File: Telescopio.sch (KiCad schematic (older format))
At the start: 18 parts, among them CON1 BARREL_JACK, P1 CONN_01X03, P10 CONN_01X08, P12 CONN_01X04, P13 CONN_01X04, P2 CONN_01X03, P3 CONN_01X05, P4 CONN_01X19, P5 CONN_01X19, P50 CONN_01X04, P51 CONN_01X10, P7 CONN_01X08, P8 CONN_01X08, P9 CONN_01X08

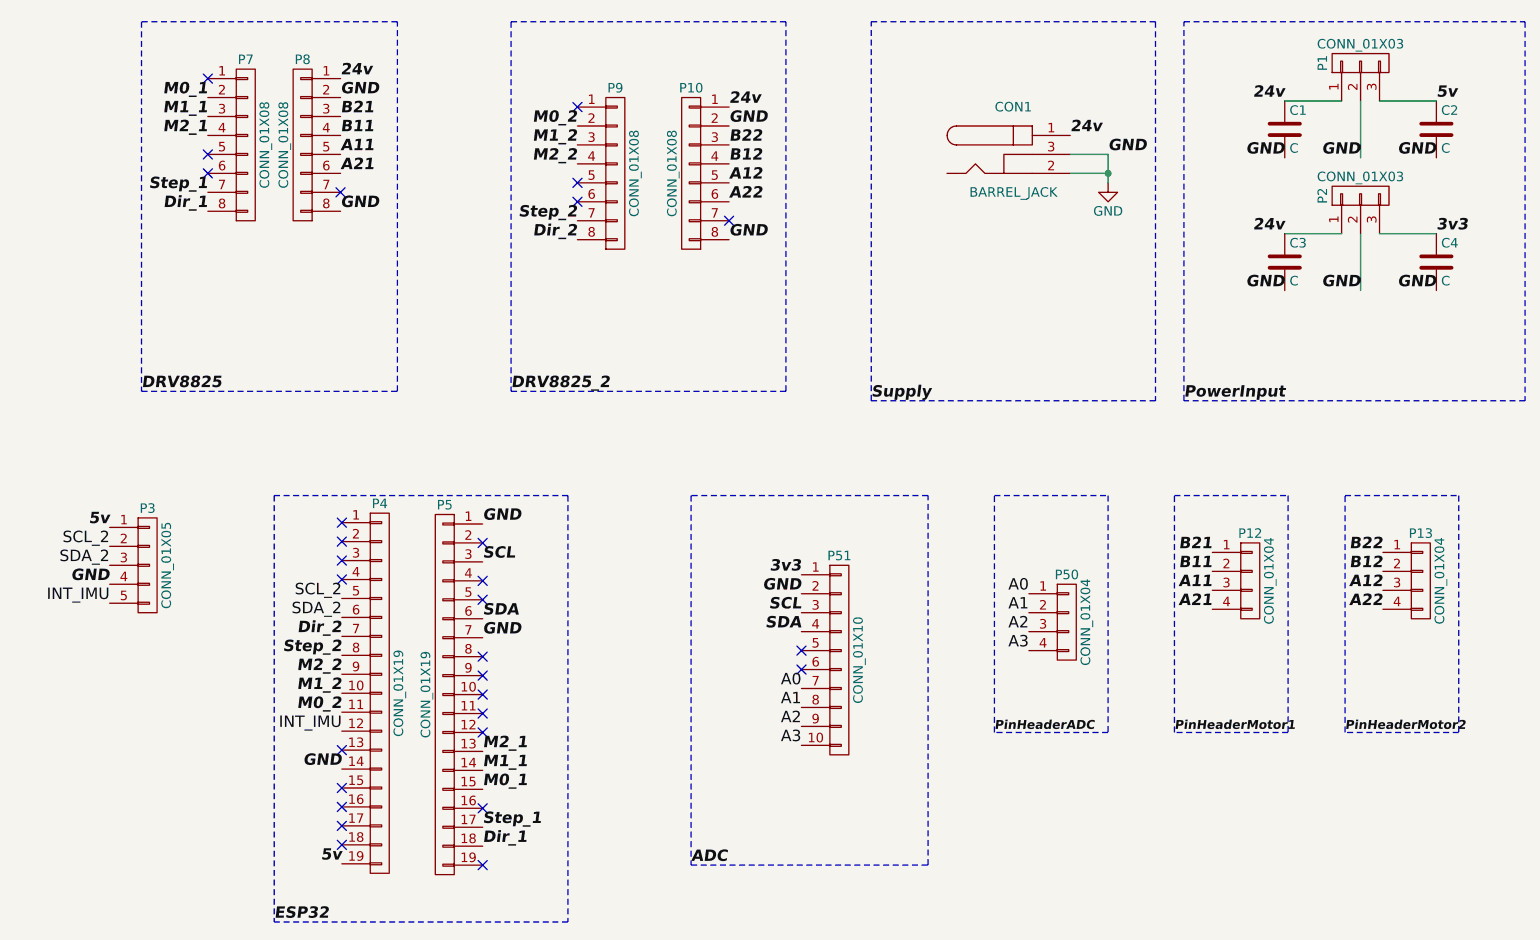
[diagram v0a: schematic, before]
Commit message: button reset
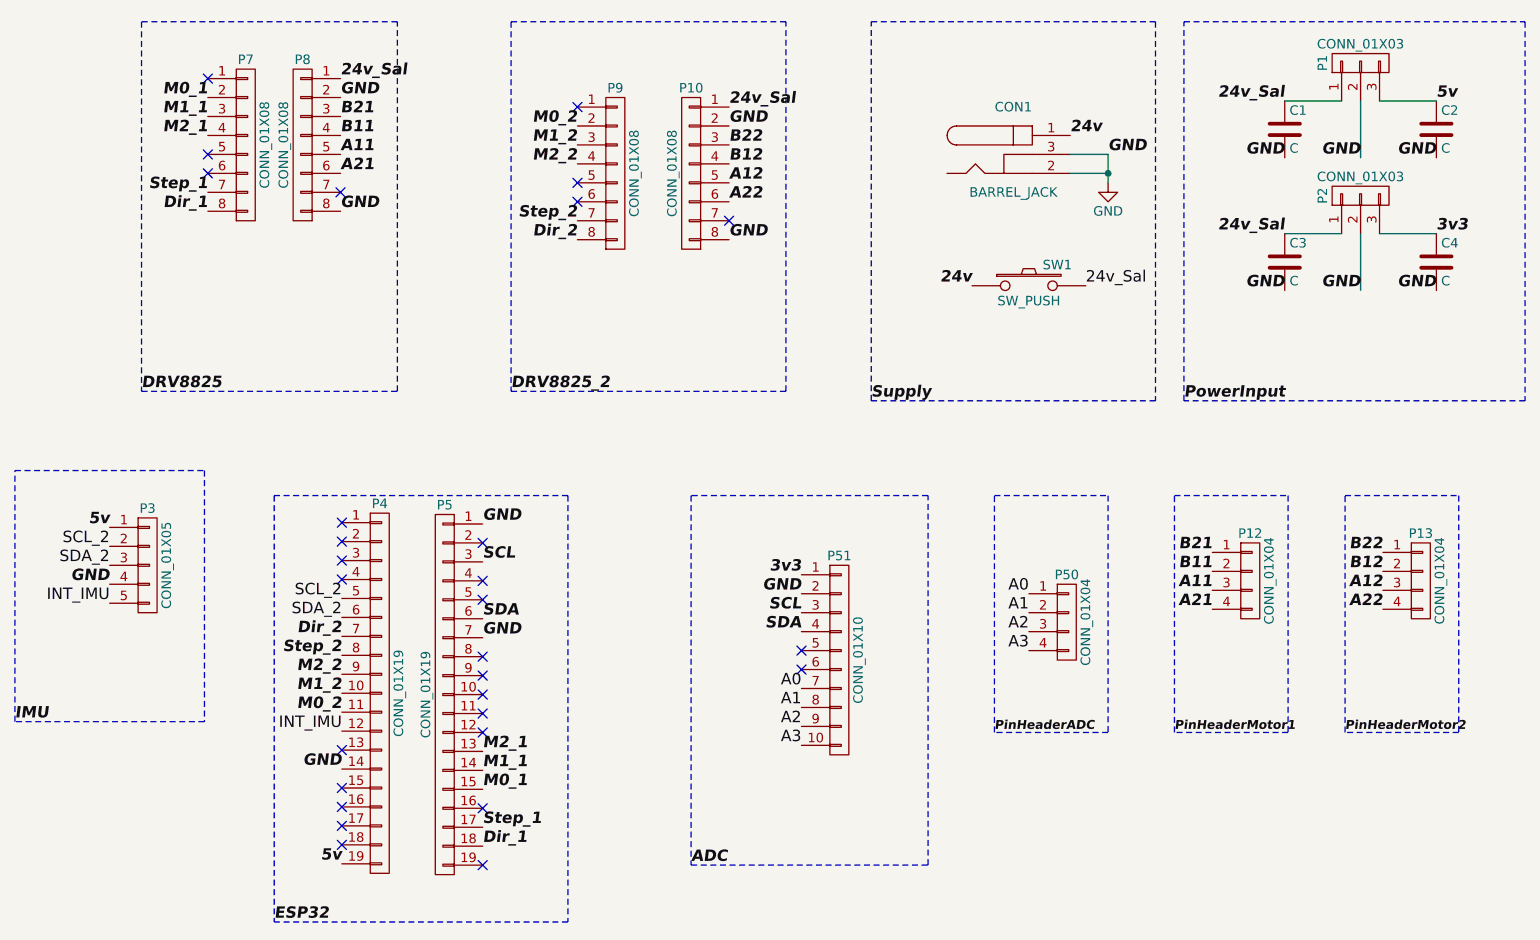
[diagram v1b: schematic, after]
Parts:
- added SW1: SW_PUSH, Buttons_Switches_ThroughHole:SW_PUSH, symbol SW_PUSH
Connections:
- net 24v: now also SW1.1; no longer C1.1, C3.1, P1.1 (P1), P10.1 (P1), P2.1 (P1), P8.1 (P1)
- new net 24v_Sal: C1.1, C3.1, P1.1 (P1), P10.1 (P1), P2.1 (P1), P8.1 (P1), SW1.2
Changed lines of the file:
@@
 24v
 Text Label 7450 1750 2    60   Italic 12
-24v
+24v_Sal
 Text Label 7450 2450 2    60   Italic 12
-24v
+24v_Sal
 Text Label 7850 2050 2    60   Italic 12
 GND
@@
 PowerInput
 Text Label 2468 1632 0    60   Italic 12
-24v
+24v_Sal
 Text Label 4518 1782 0    60   Italic 12
-24v
+24v_Sal
 Text Label 2468 1732 0    60   Italic 12
 GND
@@
 Text Label 2475 5075 2    60   ~ 0
 INT_IMU
+Wire Notes Line
+	750  3700 1750 3700
+Wire Notes Line
+	1750 3700 1750 5025
+Wire Notes Line
+	1750 5025 750  5025
+Wire Notes Line
+	750  5025 750  3700
+Text Label 750  5025 0    60   Italic 12
+IMU
+$Comp
+L SW_PUSH SW1
+U 1 1 59457ED8
+P 6100 2725
+F 0 "SW1" H 6250 2835 50  0000 C CNN
+F 1 "SW_PUSH" H 6100 2645 50  0000 C CNN
+F 2 "Buttons_Switches_ThroughHole:SW_PUSH" H 6100 2725 50  0001 C CNN
+F 3 "" H 6100 2725 50  0000 C CNN
+	1    6100 2725
+	1    0    0    -1
+$EndComp
+Text Label 5800 2725 2    60   Italic 12
+24v
+Text Label 6400 2725 0    60   ~ 0
+24v_Sal
 $EndSCHEMATC

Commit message: modifed pcb for testing
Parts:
- removed C1, C2, C3, C4: C, Capacitors_ThroughHole:C_Radial_D5_L11_P2.5, symbol C
- removed CON1: BARREL_JACK, Connect:BARREL_JACK, symbol BARREL_JACK
- removed P1, P2: CONN_01X03, TO_SOT_Packages_THT:TO-220_Neutral123_Vertical_LargePads, symbol CONN_01X03
- removed P10, P7, P8, P9: CONN_01X08, Pin_Headers:Pin_Header_Straight_1x08, symbol CONN_01X08
- removed P12, P13, P50: CONN_01X04, Sockets_MOLEX_KK-System:Socket_MOLEX-KK-RM3-96mm_Lock_4pin_straight, symbol CONN_01X04
- removed P3: CONN_01X05, Pin_Headers:Pin_Header_Straight_1x05, symbol CONN_01X05
- removed P51: CONN_01X10, Pin_Headers:Pin_Header_Straight_1x10, symbol CONN_01X10
- removed SW1: SW_PUSH, Buttons_Switches_ThroughHole:SW_PUSH, symbol SW_PUSH
- added H1: Temp_humidity, Pin_Headers:Pin_Header_Straight_1x04, symbol Conn_01x04
- added J1: ScaleL, Pin_Headers:Pin_Header_Straight_1x04, symbol Conn_01x04
- added J2: Scale, Pin_Headers:Pin_Header_Straight_1x06, symbol Conn_01x06
- added M1: Conn_01x09, Pin_Headers:Pin_Header_Straight_1x09, symbol Conn_01x09
- added S1: Shifter, Pin_Headers:Pin_Header_Straight_1x06, symbol Conn_01x06
- added S2: ShifterR, Pin_Headers:Pin_Header_Straight_1x06, symbol Conn_01x06
- added S3: Conn_01x06, Pin_Headers:Pin_Header_Straight_1x06, symbol Conn_01x06
- added Z1: Buzzer, Pin_Headers:Pin_Header_Straight_1x02, symbol Conn_01x02
- added Z2: Motor, Pin_Headers:Pin_Header_Straight_1x02, symbol Conn_01x02
- P4: value CONN_01X19 -> ESP_32
- P5: value CONN_01X19 -> esp_lora
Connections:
- net M0_2 is gone; now on net SCL: P4.11 (P11)
- net GND: now also P4.4 (P4), S2.5 (Pin_5), Z1.2 (Pin_2), Z2.1 (Pin_1); no longer P4.14 (P14), P5.1 (P1), P5.7 (P7)
- net SCL: now also H1.4 (Pin_4); no longer P5.3 (P3)
- net SDA: now also P4.18 (P18), H1.3 (Pin_3); no longer P5.6 (P6)
- net GND1: now reaches P5.19 (P19)
- net GND1: now also J1.4 (Pin_4)
- net at P5.2 (P2): now also Z1.1 (Pin_1)
- net GND2: now reaches P4.1 (P1)
- net GND2: now also H1.1 (Pin_1)
- net 5v1: now reaches P4.2 (P2)
- net 5v1: now also H1.2 (Pin_2), S1.6 (Pin_6)
- net 3v: now reaches P4.3 (P3)
- net 3v: now also S2.6 (Pin_6)
- net 5v: no longer names the net of P4.19 (P19)
- net Dir_1 renamed VCC
- net VCC: now also J1.1 (Pin_1)
- net Dir_2: no longer names the net of P4.7 (P7)
- net INT_IMU: no longer names the net of P4.12 (P12)
- net M0_1: no longer names the net of P5.15 (P15)
- net M1_1: no longer names the net of P5.14 (P14)
- net M1_2: no longer names the net of P4.10 (P10)
- net M2_1: no longer names the net of P5.13 (P13)
- net M2_2: no longer names the net of P4.9 (P9)
- net SCL_2: no longer names the net of P4.5 (P5)
- net SDA_2: no longer names the net of P4.6 (P6)
- net Step_1: no longer names the net of P5.17 (P17)
- net Step_2 renamed M0
- net M0: now also S2.1 (Pin_1)
- new net A+: J2.3 (Pin_3)
- new net A-: J2.4 (Pin_4)
- new net DT: J1.3 (Pin_3), P5.1 (P1)
- new net E+: J2.6 (Pin_6)
- new net E-: J2.5 (Pin_5)
- new net M1: S1.1 (Pin_1), Z2.2 (Pin_2)
- new net SCK: J1.2 (Pin_2), P5.3 (P3)
- no-connect marks 29 -> 54
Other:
- moved on the sheet: P4

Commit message: general fixes
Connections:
- net GND1 is gone; now on net GND: J1.4 (Pin_4), P5.19 (P19)
- net GND2 is gone; now on net GND: H1.1 (Pin_1), P4.1 (P1)
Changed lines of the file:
@@
 ESP32_lora
 Text Label 5410 2310 0    60   Italic 12
-GND1
+GND
 NoConn ~ 4660 3910
 NoConn ~ 4660 3810
@@
 3v1
 Text Label 4660 2310 2    60   Italic 12
-GND2
+GND
 Text Label 3685 4590 0    60   Italic 12
 M0
@@
 NoConn ~ 2985 4490
 Text Label 6535 3105 2    60   Italic 12
-GND1
+GND
 Text Label 4660 2410 2    60   Italic 12
 5v1
@@
 SDA
 Text Label 4030 1835 3    60   Italic 12
-GND2
+GND
 Text Label 3930 1835 3    60   Italic 12
 5v1

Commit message: added scale out
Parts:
- added J?: ScaleOut, Pin_Headers:Pin_Header_Straight_1x06, symbol Conn_01x06
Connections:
- net A+: now also J?.4 (Pin_4)
- net A-: now also J?.3 (Pin_3)
- net E+: now also J?.1 (Pin_1)
- net E-: now also J?.2 (Pin_2)
- no-connect marks 54 -> 50
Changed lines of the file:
@@
 	-1   0    0    1
 $EndComp
-NoConn ~ 7235 2805
-NoConn ~ 7235 2905
-NoConn ~ 7235 3005
-NoConn ~ 7235 3105
 NoConn ~ 4660 3110
 Text Label 6535 2805 2    60   Italic 12
@@
 Text Label 3025 4705 3    60   ~ 0
 GND
+$Comp
+L Conn_01x06 J?
+U 1 1 5A5781D2
+P 7740 2885
+F 0 "J?" H 7740 3185 50  0000 C CNN
+F 1 "ScaleOut" V 7840 2535 50  0000 L CNN
+F 2 "Pin_Headers:Pin_Header_Straight_1x06" H 7740 2885 50  0001 C CNN
+F 3 "" H 7740 2885 50  0001 C CNN
+	1    7740 2885
+	1    0    0    1
+$EndComp
+Wire Wire Line
+	7540 3085 7235 3105
+Wire Wire Line
+	7540 2985 7235 3005
+Wire Wire Line
+	7540 2885 7235 2905
+Wire Wire Line
+	7540 2785 7235 2805
 $EndSCHEMATC

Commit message: general fixes
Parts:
- gave numbers to parts that had none: 1
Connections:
- no-connect marks 50 -> 52
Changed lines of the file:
@@
 Text Label 4320 4410 0    60   Italic 12
 ESP32_lora
-Text Label 5410 2310 0    60   Italic 12
-GND
 NoConn ~ 4660 3910
 NoConn ~ 4660 3810
@@
 F 3 "" H 4860 3210 50  0000 C CNN
 	1    4860 3210
-	1    0    0    -1
-$EndComp
-$Comp
-L Conn_01x04 J1
-U 1 1 5A53BC44
-P 6735 2905
-F 0 "J1" H 6735 3105 50  0000 C CNN
-F 1 "ScaleL" V 6785 2905 50  0000 C TNN
-F 2 "Pin_Headers:Pin_Header_Straight_1x04" H 6735 2905 50  0001 C CNN
-F 3 "" H 6735 2905 50  0001 C CNN
-	1    6735 2905
 	1    0    0    -1
 $EndComp
@@
 	5680 2420 5410 2410
 Wire Wire Line
-	6535 3105 6535 3245
-Wire Wire Line
-	6535 3245 7475 3245
-Wire Wire Line
-	7475 3245 7455 2245
-Wire Wire Line
-	5410 2215 5410 2310
-Wire Wire Line
 	6535 2905 6005 2905
 Wire Wire Line
@@
 Wire Wire Line
 	3960 3965 3685 4090
-Wire Wire Line
-	7455 2245 5410 2215
 Wire Wire Line
 	3960 3965 3965 3575
@@
 GND
 $Comp
-L Conn_01x06 J?
+L Conn_01x06 J3
 U 1 1 5A5781D2
 P 7740 2885
-F 0 "J?" H 7740 3185 50  0000 C CNN
+F 0 "J3" H 7740 3185 50  0000 C CNN
 F 1 "ScaleOut" V 7840 2535 50  0000 L CNN
 F 2 "Pin_Headers:Pin_Header_Straight_1x06" H 7740 2885 50  0001 C CNN
@@
 Wire Wire Line
 	7540 2785 7235 2805
+$Comp
+L Conn_01x04 J1
+U 1 1 5A53BC44
+P 6735 2905
+F 0 "J1" H 6735 3105 50  0000 C CNN
+F 1 "ScaleL" V 6785 2905 50  0000 C TNN
+F 2 "Pin_Headers:Pin_Header_Straight_1x04" H 6735 2905 50  0001 C CNN
+F 3 "" H 6735 2905 50  0001 C CNN
+	1    6735 2905
+	1    0    0    -1
+$EndComp
+NoConn ~ 7540 2685
+NoConn ~ 7540 2585
+Text Label 5410 2310 0    60   Italic 12
+GND
 $EndSCHEMATC

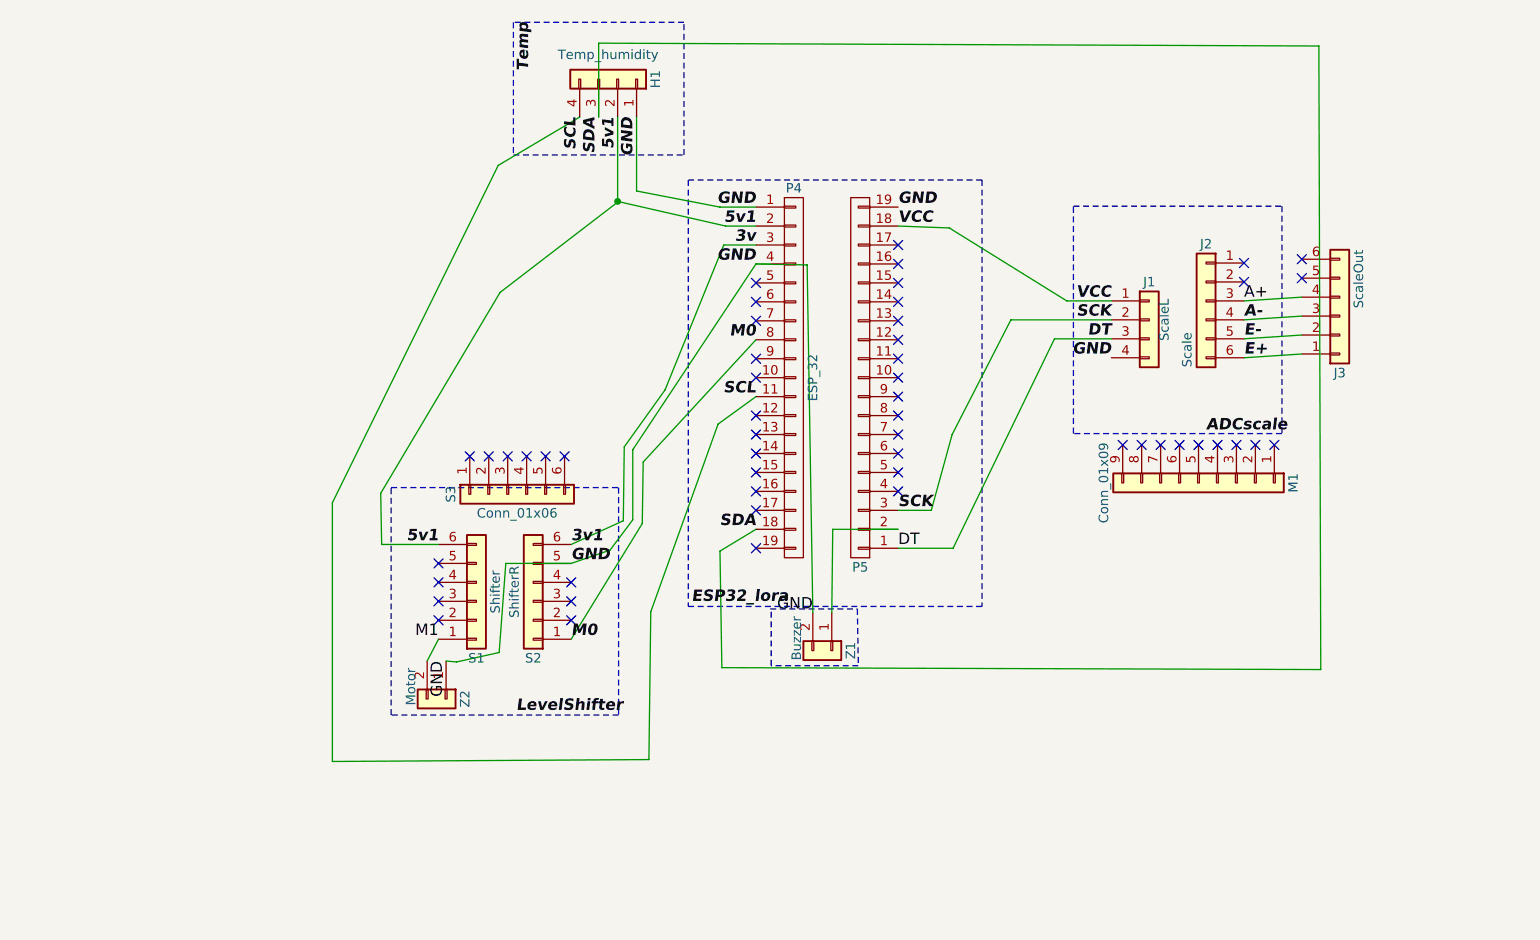
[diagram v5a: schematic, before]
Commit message: add pinheaders 2.0mm
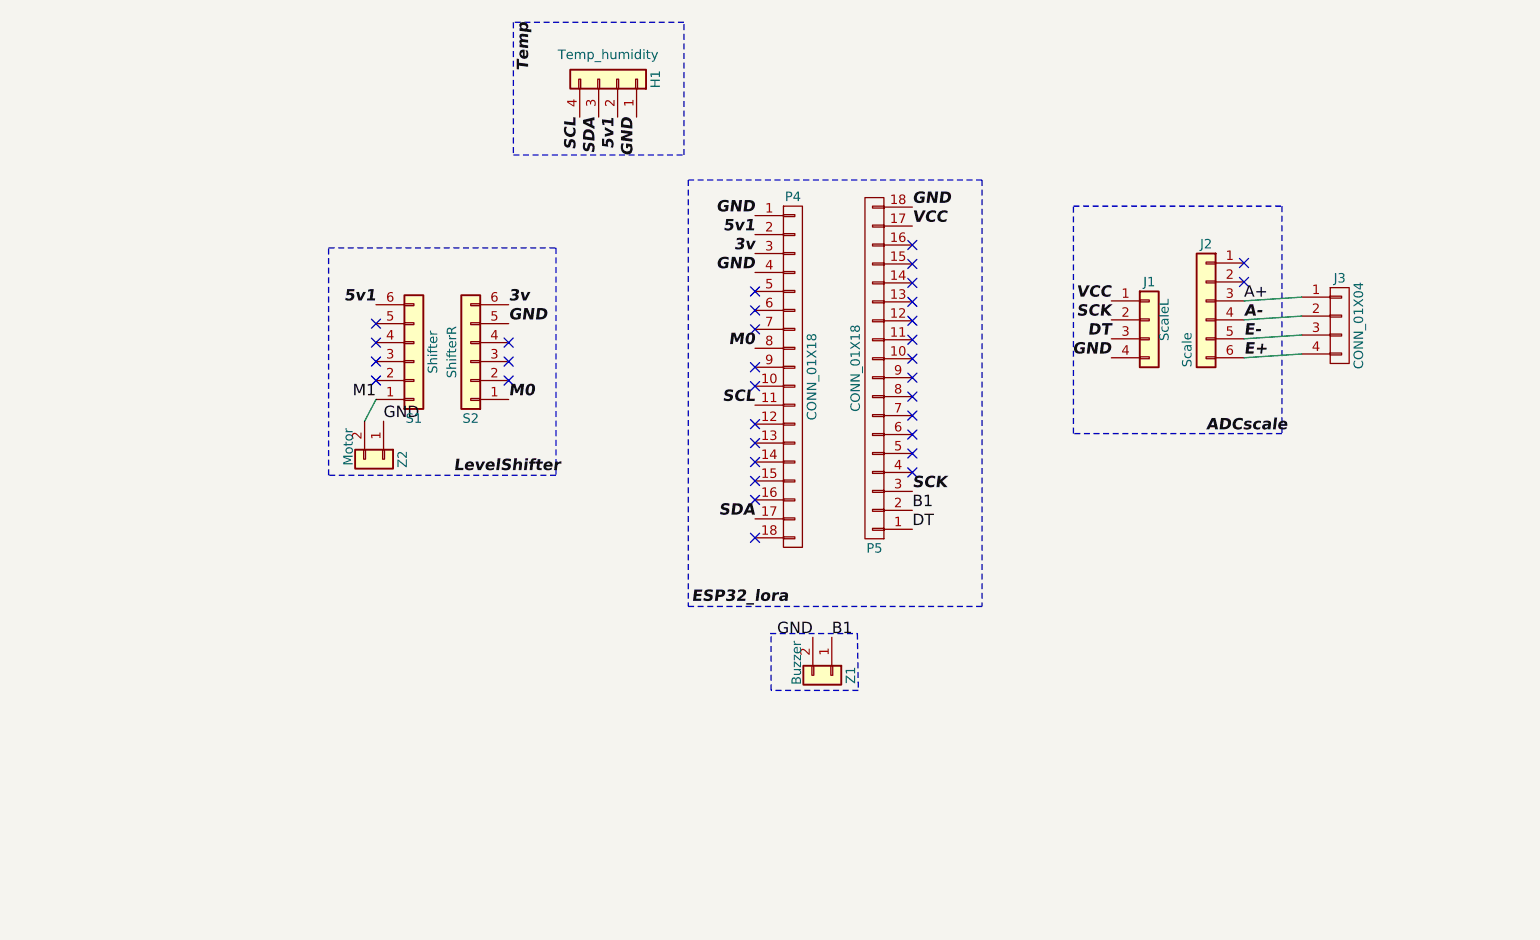
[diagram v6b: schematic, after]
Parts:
- removed J3: ScaleOut, Pin_Headers:Pin_Header_Straight_1x06, symbol Conn_01x06
- removed M1: Conn_01x09, Pin_Headers:Pin_Header_Straight_1x09, symbol Conn_01x09
- removed P4: ESP_32, Pin_Headers:Pin_Header_Straight_1x19, symbol CONN_01X19
- removed P5: esp_lora, Pin_Headers:Pin_Header_Straight_1x19, symbol CONN_01X19
- removed S3: Conn_01x06, Pin_Headers:Pin_Header_Straight_1x06, symbol Conn_01x06
- added J3: CONN_01X04, myelin-kicad:Pin_Header_Straight_1x04_Pitch2.00mm, symbol CONN_01X04
- added P4, P5: CONN_01X18, Pin_Headers:Pin_Header_Straight_1x18, symbol CONN_01X18
- H1: footprint Pin_Headers:Pin_Header_Straight_1x04 -> myelin-kicad:Pin_Header_Straight_1x04_Pitch2.00mm
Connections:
- net 3v: now also P4.3 (P3)
- net 5v1: now also P4.2 (P2)
- net A+: now also J3.1 (P1)
- net A-: now also J3.2 (P2)
- net DT: now also P5.1 (P1)
- net E+: now also J3.4 (P4)
- net E-: now also J3.3 (P3)
- net GND: now also P4.1 (P1), P4.4 (P4), P5.18 (P18)
- net M0: now also P4.8 (P8)
- net SCK: now also P5.3 (P3)
- net SCL: now also P4.11 (P11)
- net SDA: now also P4.17 (P17)
- net VCC: now also P5.17 (P17)
- net B1: now reaches Z1.1 (Pin_1)
- net B1: now also P5.2 (P2)
- no-connect marks 52 -> 33
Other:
- moved on the sheet: S1, S2, Z1, Z2
